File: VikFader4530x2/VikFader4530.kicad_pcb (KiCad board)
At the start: 2 copper layers, 24.1 x 45.8 mm, 15 parts, among them J1 vik-module-connector, J3 Conn_01x04_Pin, U1 ADS1015IDGS

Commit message: Various DRC fixes
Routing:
- net GND: track 2.73 -> 9.36 mm, vias 1 -> 2
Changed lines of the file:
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@@
+	)
+	(via
+		(at 194.8 63.74)
+		(size 0.6)
+		(drill 0.3)
+		(layers "F.Cu" "B.Cu")
+		(net 1)
 	)
 	(via
@@
 	)
 	(segment
+		(start 195.4 70.035)
+		(end 196.155 70.79)
+		(width 0.2)
+		(layer "B.Cu")
+		(net 1)
+	)
+	(segment
+		(start 194.2955 63.74)
+		(end 194.8 63.74)
+		(width 0.2)
+		(layer "B.Cu")
+		(net 1)
+	)
+	(segment
 		(start 213.758 64.55)
 		(end 211.17 64.55)
 		(width 0.2)
 		(layer "B.Cu")
+		(net 1)
+	)
+	(segment
+		(start 193.9 64.1355)
+		(end 194.2955 63.74)
+		(width 0.2)
+		(layer "B.Cu")
+		(net 1)
+	)
+	(segment
+		(start 194.9 64.9125)
+		(end 194.9 63.84)
+		(width 0.2)
+		(layer "B.Cu")
+		(net 1)
+	)
+	(segment
+		(start 195.9 69.2125)
+		(end 195.9 70.535)
+		(width 0.2)
+		(layer "B.Cu")
+		(net 1)
+	)
+	(segment
+		(start 195.4 69.2125)
+		(end 195.4 70.035)
+		(width 0.2)
+		(layer "B.Cu")
+		(net 1)
+	)
+	(segment
+		(start 193.9 64.9125)
+		(end 193.9 64.1355)
+		(width 0.2)
+		(layer "B.Cu")
+		(net 1)
+	)
+	(segment
+		(start 194.9 63.84)
+		(end 194.8 63.74)
+		(width 0.2)
+		(layer "B.Cu")
+		(net 1)
+	)
+	(segment
+		(start 195.9 70.535)
+		(end 196.155 70.79)
+		(width 0.2)
+		(layer "B.Cu")

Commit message: All three models refactored to MOSFET setup
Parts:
- removed REF**: vik-logo-small, vik-fader:vik-logo-small
- added J2: Conn_01x06_Pin, Connector_PinHeader_2.54mm:PinHeader_1x06_P2.54mm_Vertical, B.Cu at (203.4, 60.4)
- added J4: Conn_01x01_Pin, MountingHole:MountingHole_2.2mm_M2_DIN965_Pad_TopOnly, B.Cu at (199.4, 63.8)
- added JP1: 0x48, Jumper:SolderJumper-2_P1.3mm_Bridged_RoundedPad1.0x1.5mm, B.Cu at (198.8, 72.4)
- added JP2: 0x49, Jumper:SolderJumper-2_P1.3mm_Open_RoundedPad1.0x1.5mm, B.Cu at (198.8, 74.9)
- added JP3: 0x4A, Jumper:SolderJumper-2_P1.3mm_Open_RoundedPad1.0x1.5mm, B.Cu at (198.8, 77.4)
- added JP4: 0x4B, Jumper:SolderJumper-2_P1.3mm_Open_RoundedPad1.0x1.5mm, B.Cu at (198.8, 79.9)
- added Q1: DMG2305UX, Package_TO_SOT_SMD:SOT-23, B.Cu at (203.7, 53.2)
- added R7: 1kΩ, Resistor_SMD:R_0603_1608Metric, B.Cu at (206.6, 53.8)
- added R8: 100kΩ, Resistor_SMD:R_0603_1608Metric, B.Cu at (208.1, 53.8)
- added R9: 10kΩ, Resistor_SMD:R_0805_2012Metric, B.Cu at (213.4, 58.4)
- J3: value Conn_01x04_Pin -> Conn_01x01_Pin; footprint Connector_PinHeader_2.00mm:PinHeader_1x04_P2.00mm_Vertical -> MountingHole:MountingHole_2.2mm_M2_DIN965_Pad_TopOnly; moved to B.Cu
- R2, R3: footprint Capacitor_SMD:C_0603_1608Metric -> Resistor_SMD:R_0805_2012Metric
- R4, R6: footprint Capacitor_SMD:C_0603_1608Metric -> Resistor_SMD:R_0603_1608Metric
- moved R2 14.7 mm to (211.5, 58.4), turned to -90 degrees
- moved R3 14.3 mm to (209.5, 58.4), turned to -90 degrees
- moved J3 14.1 mm to (199.4, 60.6), turned to 180 degrees
- moved J1 0.46 mm to (212.2, 66.7)
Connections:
- J3 pad 1: +3V3 -> AIN2
- R1 pad 1: +3V3 -> FET-OUT
- R5 pad 1: +3V3 -> FET-OUT
- U1 pad 1: GND -> Net-(JP1-B)
- U1 pad 2: unconnected-(U1-ALERT/RDY-Pad2) -> GP1
- U1 pad 6: GND -> AIN2
- U1 pad 7: GND -> AIN3
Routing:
- net GP1: track 0.00 -> 42.0 mm, vias 0 -> 4
- net GP2: track 0.00 -> 33.3 mm, vias 0 -> 1
- net FET-OUT: track 0.00 -> 22.2 mm
- net Net-(JP1-B): track 0.00 -> 20.4 mm
- net AIN2: track 0.00 -> 16.2 mm, vias 0 -> 2
- net AIN3: track 0.00 -> 12.1 mm, vias 0 -> 2
- net SCL: track 39.9 -> 49.7 mm
- net +3V3: track 79.0 -> 69.6 mm, vias 4 -> 5
- net SDA: track 37.4 -> 46.0 mm
- net Net-(Q1-G): track 0.00 -> 3.97 mm
- net POT-IN1: track 27.2 -> 30.9 mm
- net GND: track 9.36 -> 12.7 mm, vias 2 -> 6
- net POT-OUT1: track 2.73 -> 3.52 mm, vias 0 -> 1
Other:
- board text added: "FET"
- board text added: "RDY"

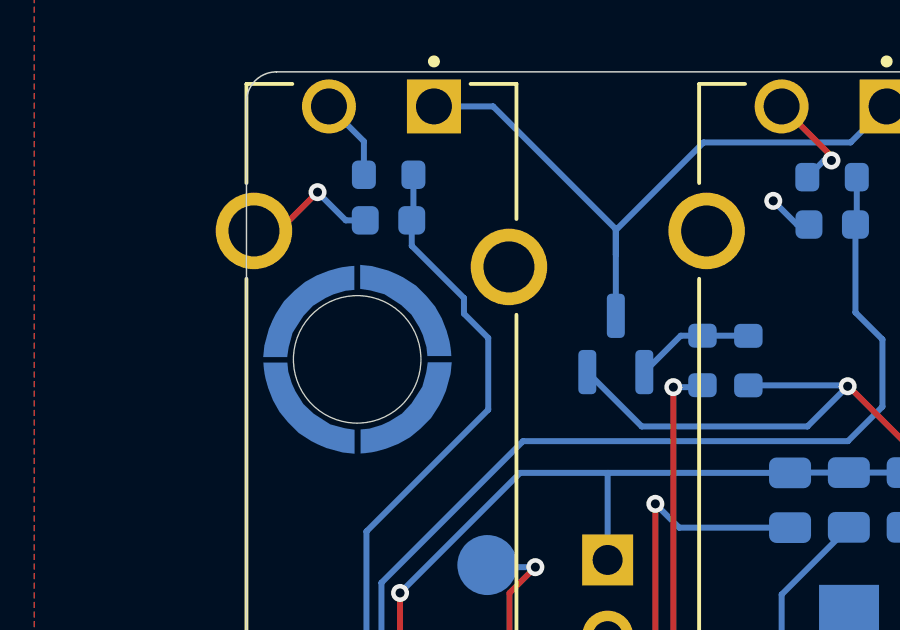
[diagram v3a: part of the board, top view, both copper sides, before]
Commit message: Final cleanup of JLC part assignmet
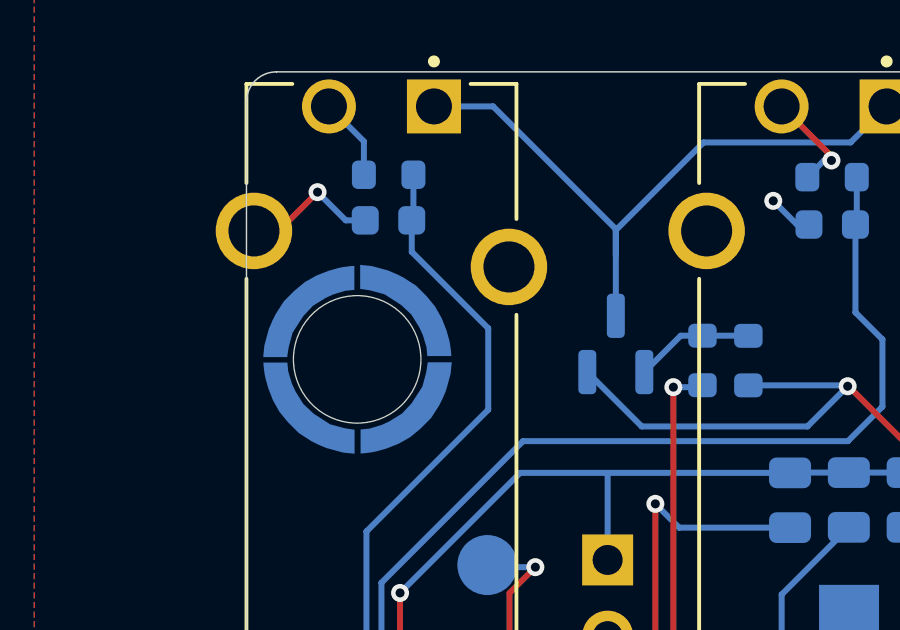
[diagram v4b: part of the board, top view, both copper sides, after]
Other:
- board text added: "A2"
- board text added: "A3"
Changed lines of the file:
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@@
 		(tags "mounting hole 2.2mm m2 din965")
 		(property "Reference" "J3"
-			(at 0 2.9 0)
-			(layer "B.SilkS")
+			(at 1.73 1.07 0)
+			(layer "User.1")
 			(effects
 				(font
@@
 		)
 		(property "Value" "0x4A"
-			(at -3.29 -0.01 0)
+			(at -3.22 0.58 0)
 			(layer "B.SilkS")
 			(effects
@@
 		(tags "mounting hole 2.2mm m2 din965")
 		(property "Reference" "J4"
-			(at 0 2.9 0)
-			(layer "B.SilkS")
+			(at 1.57 1.56 0)
+			(layer "User.1")
 			(effects
 				(font
@@
 		)
 		(property "Value" "0x48"
-			(at 3.27 0.06 0)
+			(at 3.21 -0.67 0)
 			(layer "B.SilkS")
 			(effects
@@
 		)
 		(property "Value" "0x4B"
-			(at -3.31 -0.08 0)
+			(at -3.31 0.54 0)
 			(layer "B.SilkS")
 			(effects
@@
 		)
 		(property "Value" "0x49"
-			(at -3.25 -0.05 0)
+			(at -3.22 0.6 0)
 			(layer "B.SilkS")
 			(effects
@@
 		)
 	)
+	(gr_text "A2"
+		(at 199.94 59.34 0)
+		(layer "B.SilkS")
+		(effects
+			(font
+				(size 0.5 0.5)
+				(thickness 0.12)
+				(bold yes)
+			)
+			(justify left bottom mirror)
+		)
+	)
 	(gr_text "GND"
 		(at 201.94 62.22 90)
@@
 		)
 	)
+	(gr_text "A3"
+		(at 199.94 62.56 0)
+		(layer "B.SilkS")
+		(effects
+			(font
+				(size 0.5 0.5)
+				(thickness 0.12)
+				(bold yes)
+			)
+			(justify left bottom mirror)
+		)
+	)
 	(gr_text "SCL"
 		(at 201.93 67.48 90)
@@
 	)
 	(segment
-		(start 198.65 52.22)
-		(end 199.46 53.03)
+		(start 199.46 55.42)
+		(end 195.4 59.48)
 		(width 0.2)
 		(layer "B.Cu")
@@
 	)
 	(segment
-		(start 196.91 49.11)
-		(end 196.91 49.96)
+		(start 199.46 52.71)
+		(end 199.46 55.42)
 		(width 0.2)
 		(layer "B.Cu")
@@
 	)
 	(segment
-		(start 196.91 49.96)
-		(end 198.65 51.7)
+		(start 196.91 49.11)
+		(end 196.91 50.16)
 		(width 0.2)
 		(layer "B.Cu")
@@
 	)
 	(segment
-		(start 196.965 49.055)
-		(end 196.91 49.11)
+		(start 195.4 59.48)
+		(end 195.4 64.9125)
 		(width 0.2)
 		(layer "B.Cu")
@@
 	)
 	(segment
-		(start 198.65 51.7)
-		(end 198.65 52.22)
+		(start 196.91 50.16)
+		(end 199.46 52.71)
 		(width 0.2)
 		(layer "B.Cu")
@@
 	)
 	(segment
-		(start 199.46 53.03)
-		(end 199.46 55.42)
+		(start 196.965 49.055)
+		(end 196.91 49.11)
 		(width 0.2)
 		(layer "B.Cu")
@@
 		(width 0.2)
 		(layer "B.Cu")
-		(net 2)
-	)
-	(segment
-		(start 199.46 55.42)
-		(end 195.4 59.48)
-		(width 0.2)
-		(layer "B.Cu")
-		(net 2)
-	)
-	(segment
-		(start 195.4 59.48)
-		(end 195.4 64.9125)
-		(width 0.2)
-		(layer "B.Cu")
